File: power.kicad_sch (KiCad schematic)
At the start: 128 parts, among them Q2 BC817-25W, Q3 DZDH0401DW, Q4 DZDH0401DW, Q5 SI7613DN-T1-GE3, Q6 SI7613DN-T1-GE3, U1 LT8350RV#PBF, U2 MP2386GG, U3 TPS65983BAZBHR

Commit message: Updated power diagram
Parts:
- added U?: LM1117MP-25NOPB, antmicro-footprints:SOT-223, symbol antmicroPMICVoltageRegulatorsLinear:LM1117MP-25NOPB
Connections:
- new net: U?.2 (VOUT), U?.4 (VOUT)
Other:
- note added: "12V source selection"
- note added: "3V3 Fan controller"
- note added: "PCIE power enable"
- moved on the sheet: C20, C21, C22, C23, C31, C34, C35, C36, C37, C39, C42, C45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

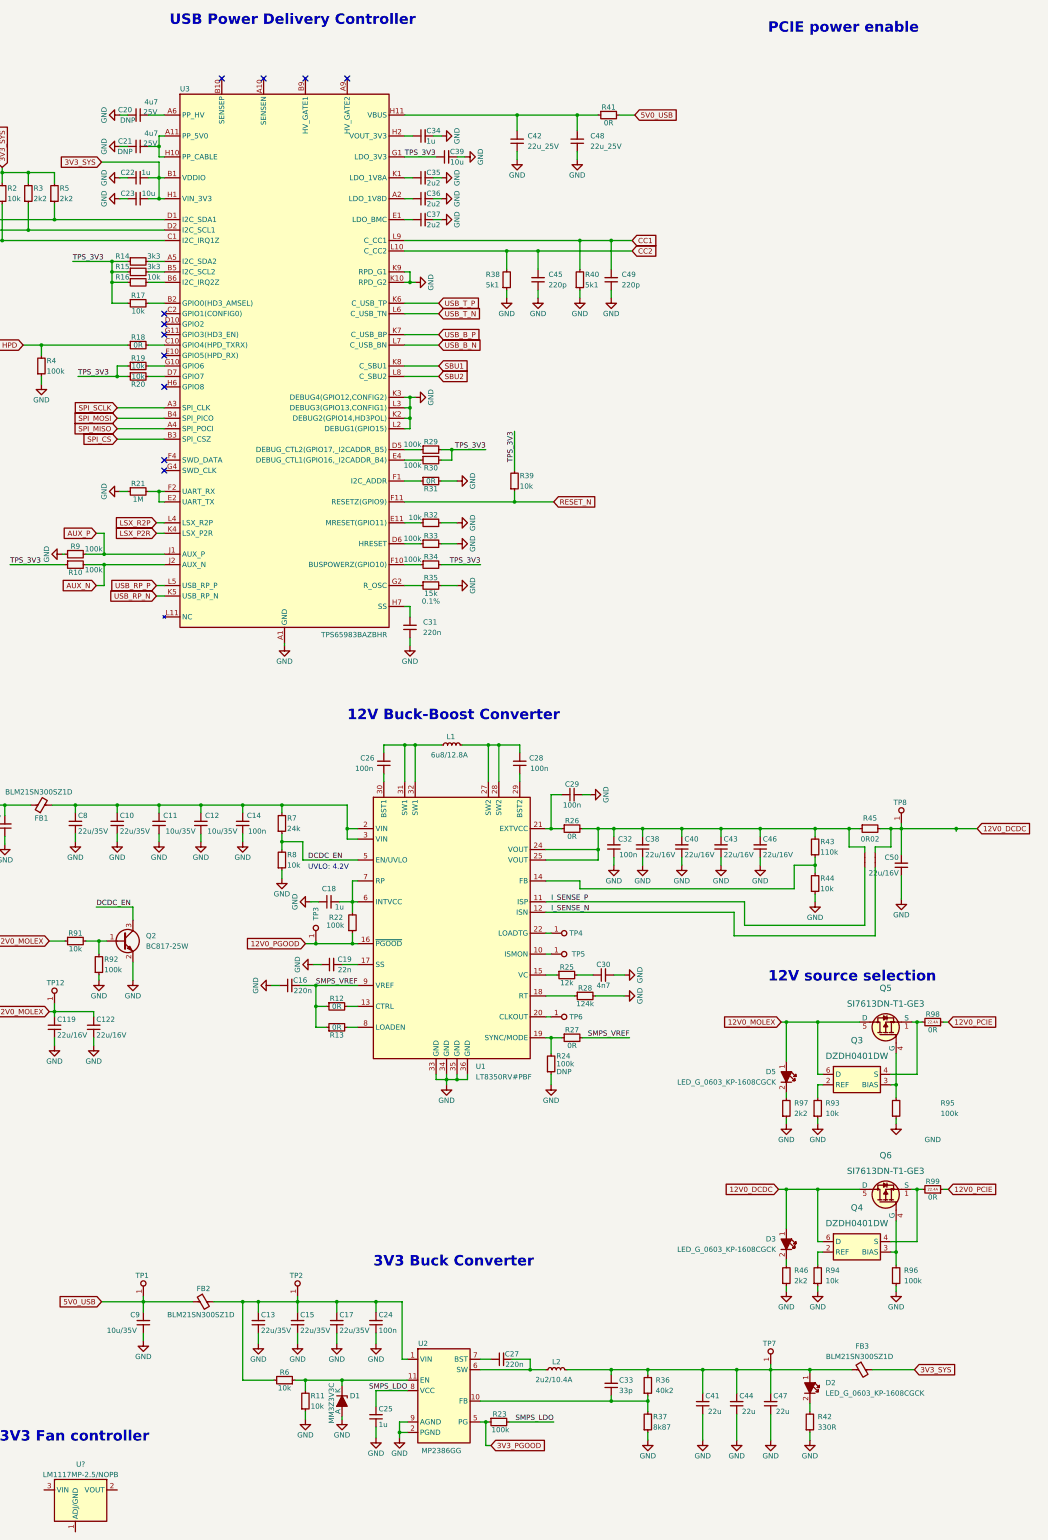
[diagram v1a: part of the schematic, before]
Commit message: Added switches for toggling PCIe power
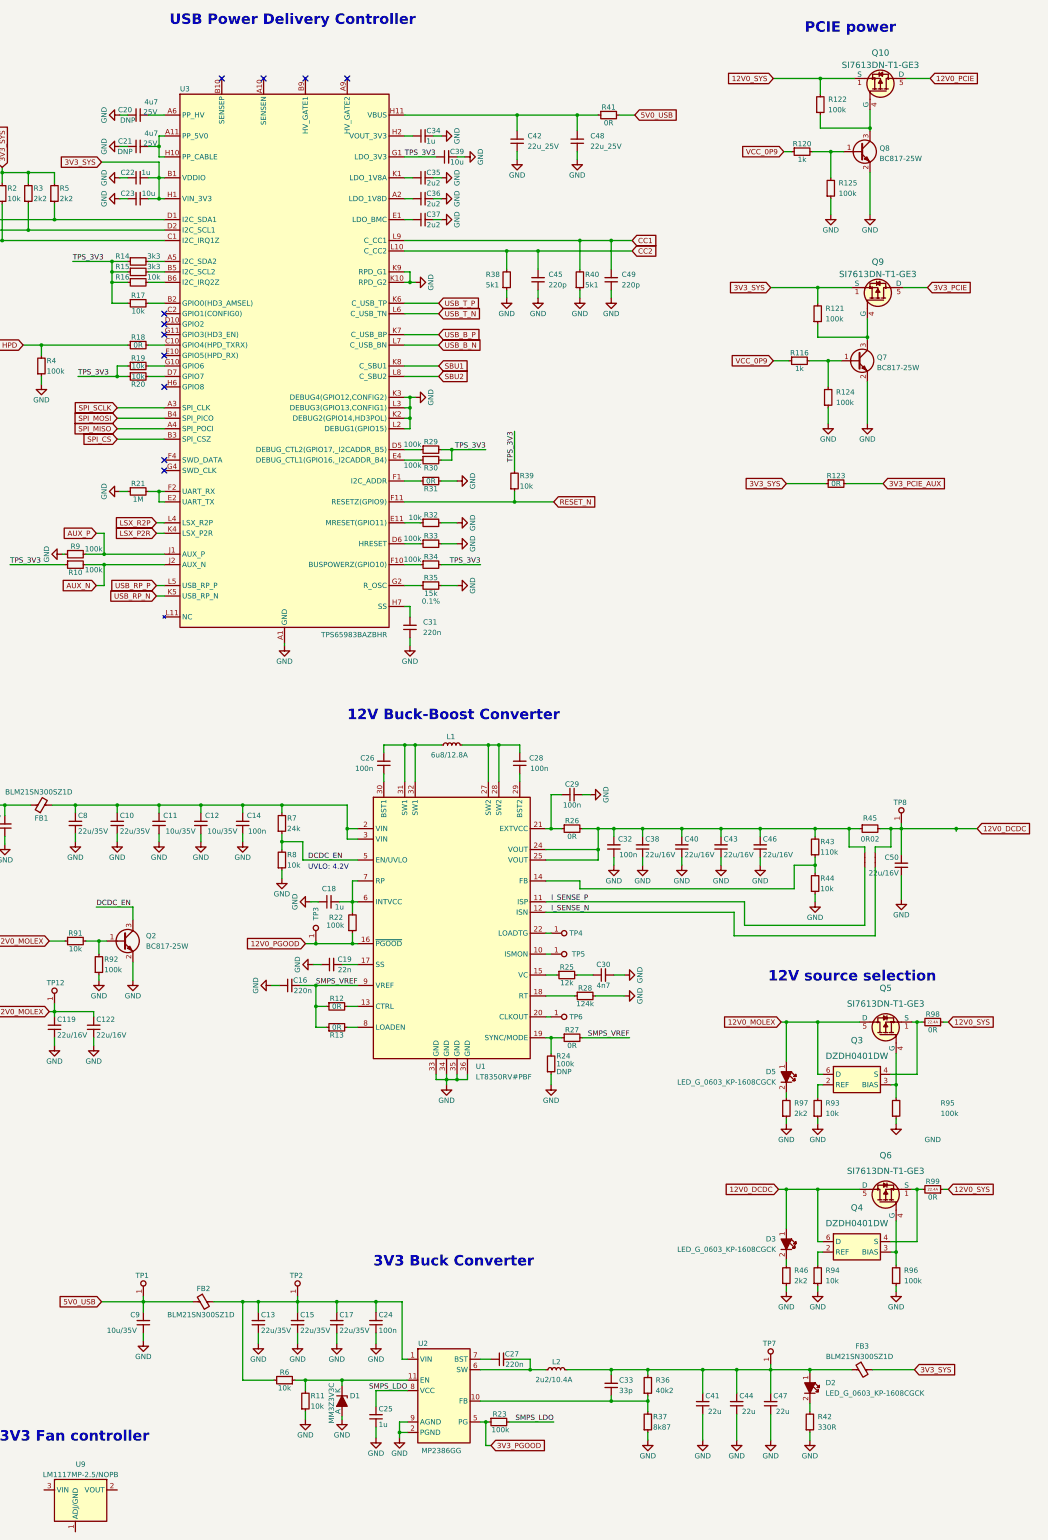
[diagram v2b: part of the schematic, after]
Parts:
- added Q10, Q9: SI7613DN-T1-GE3, antmicro-footprints:Vishay_PowerPAK_1212-8_Single, symbol antmicroTransistorsFETsMOSFETsSingle:SI7613DN-T1-GE3
- added Q7, Q8: BC817-25W, antmicro-footprints:SOT-323, symbol antmicroTransistorsBipolarSingle:BC817-25W
- added R116, R120: R_1k_0402, antmicro-footprints:R_0402_1005Metric, symbol antmicroResistors0402:R_1k_0402
- added R121, R122, R124, R125: R_100k_0402, antmicro-footprints:R_0402_1005Metric, symbol antmicroResistors0402:R_100k_0402
- added R123: R_0R_0402, antmicro-footprints:R_0402_1005Metric, symbol antmicroResistors0402:R_0R_0402
- gave numbers to parts that had none: 1
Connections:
- net 12V0_PCIE: now also Q10.5 (D); no longer R98.1, R99.1
- net 3V3_SYS: now also Q9.1 (S), Q9.2 (S), Q9.3 (S), R121.2, R123.1
- net GND: now also Q7.2 (E), Q8.2 (E), R124.1, R125.1
- new net: Q7.1 (B), R116.2, R124.2
- new net: Q7.3 (C), Q9.4 (G), R121.1
- new net: Q8.1 (B), R120.2, R125.2
- new net: Q10.4 (G), Q8.3 (C), R122.1
- new net 12V0_SYS: Q10.1 (S), Q10.2 (S), Q10.3 (S), R122.2, R98.1, R99.1
- new net 3V3_PCIE: Q9.5 (D)
- new net 3V3_PCIE_AUX: R123.2
- new net VCC_0P9: R116.1, R120.1
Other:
- note added: "PCIE power"
- note removed: "PCIE power enable"
